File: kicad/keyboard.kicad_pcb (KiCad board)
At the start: 2 copper layers, 141 x 130.1 mm, 70 parts

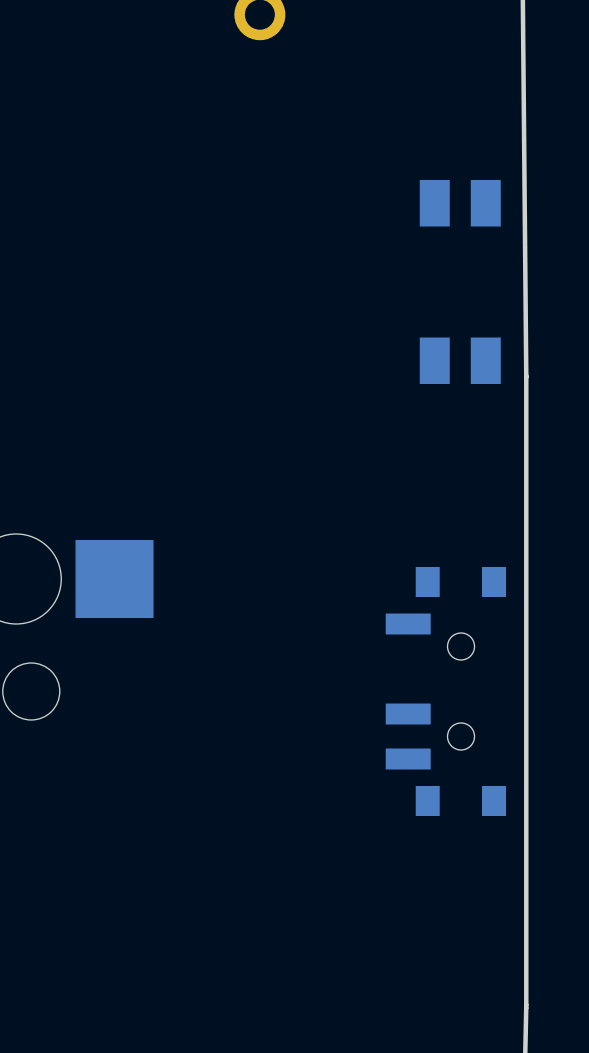
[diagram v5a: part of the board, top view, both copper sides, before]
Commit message: Move power/reset switches to Front; use detailed encoder WRL model
- power_switch and reset switch: side B -> F so they mount on the front
  (opposite the choc keys/hotswaps) and are accessible from that side.
- Replace crude Cosmos key-evqwgd001.step block with the detailed
  switch-evqwgd001 mesh converted to WRL. kicad-cli's raytracer does not
  render STL, so the STL was converted to VRML (coords pre-scaled by
  1/2.54 to compensate for KiCad's WRL unit factor). The encoder now
  renders as a realistic EVQWGD001 with visible roller wheel.
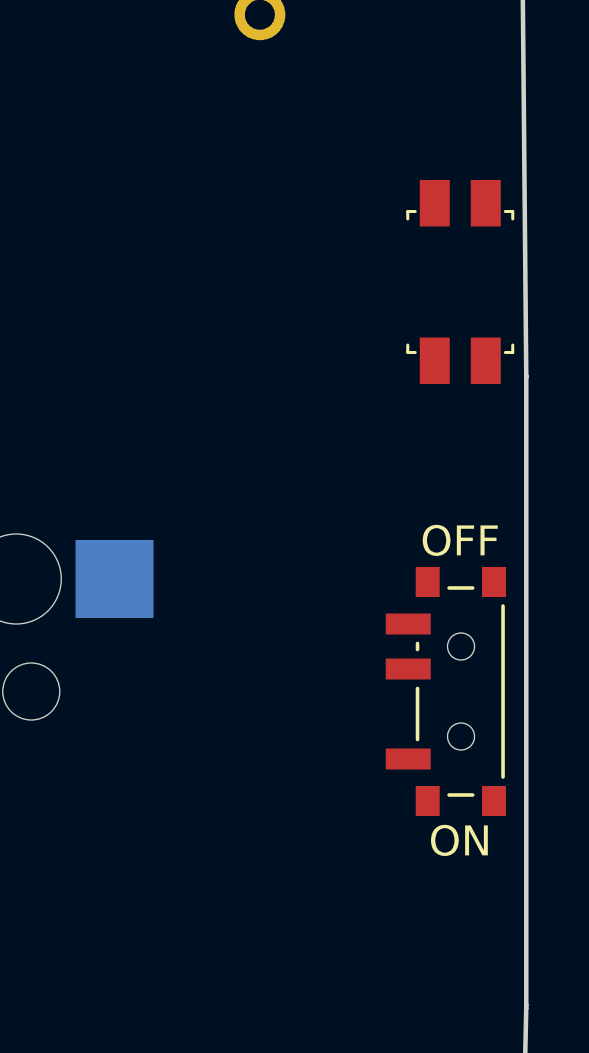
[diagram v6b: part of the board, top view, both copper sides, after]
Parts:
- PWR1, RST1: moved to F.Cu
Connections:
- PWR1 pad 1: (no net) -> BAT_P
- PWR1 pad 3: BAT_P -> (no net)
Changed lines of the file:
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@@
       (pad "D" thru_hole circle (at 5.625 3.81 0) (size 1.6 1.6) (drill 0.9) (layers "*.Cu" "*.Mask") (net 3 "GND"))
       (pad "" np_thru_hole circle (at 5.625 6.3 0) (size 1.5 1.5) (drill 1.5) (layers "*.Cu" "*.Mask"))
-    (model ${KIPRJMOD}/3d_models/EVQWGD001_Encoder.step
+    (model ${KIPRJMOD}/3d_models/EVQWGD001_Encoder.wrl
       (offset (xyz 0 0 0))
       (scale (xyz 1 1 1))
@@
     )
   (footprint "ceoloide:power_switch_smd_side"
-    (layer "B.Cu")
+    (layer "F.Cu")
     (at 153.8 77.5 0)
     (property "Reference" "PWR1"
       (at -3.6 0 -90)
-      (layer "B.SilkS")
+      (layer "F.SilkS")
       hide
       (effects (font (size 1 1) (thickness 0.15)))
     )
     (attr smd)
-    (fp_line (start 2.595 -0.1) (end 1.295 -0.1) (layer "B.Fab") (stroke (width 0.1) (type solid)))
-    (fp_line (start -1.305 3.35) (end -1.305 -3.35) (layer "B.Fab") (stroke (width 0.1) (type solid)))
-    (fp_line (start 2.645 -0.15) (end 2.595 -0.1) (layer "B.Fab") (stroke (width 0.1) (type solid)))
-    (fp_line (start 2.845 -1.2) (end 2.845 -0.35) (layer "B.Fab") (stroke (width 0.1) (type solid)))
-    (fp_line (start 1.345 -1.4) (end 2.645 -1.4) (layer "B.Fab") (stroke (width 0.1) (type solid)))
-    (fp_line (start 2.845 -0.35) (end 2.645 -0.15) (layer "B.Fab") (stroke (width 0.1) (type solid)))
-    (fp_line (start 2.645 -1.4) (end 2.845 -1.2) (layer "B.Fab") (stroke (width 0.1) (type solid)))
-    (fp_line (start 1.295 -3.35) (end 1.295 3.35) (layer "B.Fab") (stroke (width 0.1) (type solid)))
-    (fp_line (start 1.295 3.35) (end -1.305 3.35) (layer "B.Fab") (stroke (width 0.1) (type solid)))
-    (fp_line (start -1.305 -3.35) (end 1.295 -3.35) (layer "B.Fab") (stroke (width 0.1) (type solid)))
-    (pad "" smd rect (at -1.085 -3.65 270) (size 1 0.8) (layers "B.Cu" "B.Paste" "B.Mask"))
-    (pad "" smd rect (at 1.125 -3.65 270) (size 1 0.8) (layers "B.Cu" "B.Paste" "B.Mask"))
-    (pad "" smd rect (at -1.085 3.65 270) (size 1 0.8) (layers "B.Cu" "B.Paste" "B.Mask"))
-    (pad "" smd rect (at 1.125 3.65 270) (size 1 0.8) (layers "B.Cu" "B.Paste" "B.Mask"))
-    (pad "1" smd rect (at -1.735 -2.25 270) (size 0.7 1.5) (layers "B.Cu" "B.Paste" "B.Mask") )
-    (pad "2" smd rect (at -1.735 0.75 270) (size 0.7 1.5) (layers "B.Cu" "B.Paste" "B.Mask") (net 45 "RAW"))
-    (pad "3" smd rect (at -1.735 2.25 270) (size 0.7 1.5) (layers "B.Cu" "B.Paste" "B.Mask") (net 82 "BAT_P"))
-    (fp_text user "PWR1" (at -3.5 0 90) (layer "B.SilkS") hide
-      (effects (font (size 1 1) (thickness 0.15)) (justify mirror))
+    (fp_line (start -1.305 -3.35) (end -1.305 3.35) (layer "F.Fab") (stroke (width 0.1) (type solid)))
+    (fp_line (start 1.295 -3.35) (end -1.305 -3.35) (layer "F.Fab") (stroke (width 0.1) (type solid)))
+    (fp_line (start 1.295 3.35) (end 1.295 -3.35) (layer "F.Fab") (stroke (width 0.1) (type solid)))
+    (fp_line (start -1.305 3.35) (end 1.295 3.35) (layer "F.Fab") (stroke (width 0.1) (type solid)))
+    (fp_line (start 2.595 0.1) (end 1.295 0.1) (layer "F.Fab") (stroke (width 0.1) (type solid)))
+    (fp_line (start 2.645 0.15) (end 2.595 0.1) (layer "F.Fab") (stroke (width 0.1) (type solid)))
+    (fp_line (start 2.845 0.35) (end 2.645 0.15) (layer "F.Fab") (stroke (width 0.1) (type solid)))
+    (fp_line (start 2.845 1.2) (end 2.845 0.35) (layer "F.Fab") (stroke (width 0.1) (type solid)))
+    (fp_line (start 2.645 1.4) (end 2.845 1.2) (layer "F.Fab") (stroke (width 0.1) (type solid)))
+    (fp_line (start 1.345 1.4) (end 2.645 1.4) (layer "F.Fab") (stroke (width 0.1) (type solid)))
+    (pad "" smd rect (at 1.125 -3.65 90) (size 1 0.8) (layers "F.Cu" "F.Paste" "F.Mask"))
+    (pad "" smd rect (at -1.085 -3.65 90) (size 1 0.8) (layers "F.Cu" "F.Paste" "F.Mask"))
+    (pad "" smd rect (at -1.085 3.65 90) (size 1 0.8) (layers "F.Cu" "F.Paste" "F.Mask"))
+    (pad "" smd rect (at 1.125 3.65 90) (size 1 0.8) (layers "F.Cu" "F.Paste" "F.Mask"))
+    (pad "1" smd rect (at -1.735 2.25 90) (size 0.7 1.5) (layers "F.Cu" "F.Paste" "F.Mask") (net 82 "BAT_P"))
+    (pad "2" smd rect (at -1.735 -0.75 90) (size 0.7 1.5) (layers "F.Cu" "F.Paste" "F.Mask") (net 45 "RAW"))
+    (pad "3" smd rect (at -1.735 -2.25 90) (size 0.7 1.5) (layers "F.Cu" "F.Paste" "F.Mask") )
+    (fp_text user "ON" (at 0 5 0) (layer "F.SilkS")
+      (effects (font (size 1 1) (thickness 0.15)))
     )
-    (fp_text user "ON" (at 0 5 0) (layer "B.SilkS")
-      (effects (font (size 1 1) (thickness 0.15)) (justify mirror))
+    (fp_text user "OFF" (at 0 -5 0) (layer "F.SilkS")
+      (effects (font (size 1 1) (thickness 0.15)))
     )
-    (fp_text user "OFF" (at 0 -5 0) (layer "B.SilkS")
-      (effects (font (size 1 1) (thickness 0.15)) (justify mirror))
-    )
-    (fp_line (start -1.425 1.4) (end -1.425 1.6) (layer "B.SilkS") (stroke (width 0.12) (type solid)))
-    (fp_line (start 0.415 3.45) (end -0.375 3.45) (layer "B.SilkS") (stroke (width 0.12) (type solid)))
-    (fp_line (start -0.375 -3.45) (end 0.415 -3.45) (layer "B.SilkS") (stroke (width 0.12) (type solid)))
-    (fp_line (start -1.425 -1.6) (end -1.425 0.1) (layer "B.SilkS") (stroke (width 0.12) (type solid)))
-    (fp_line (start 1.425 -2.85) (end 1.425 2.85) (layer "B.SilkS") (stroke (width 0.12) (type solid)))
+    (fp_line (start 0.415 -3.45) (end -0.375 -3.45) (layer "F.SilkS") (stroke (width 0.12) (type solid)))
+    (fp_line (start -0.375 3.45) (end 0.415 3.45) (layer "F.SilkS") (stroke (width 0.12) (type solid)))
+    (fp_line (start -1.425 1.6) (end -1.425 -0.1) (layer "F.SilkS") (stroke (width 0.12) (type solid)))
+    (fp_line (start 1.425 2.85) (end 1.425 -2.85) (layer "F.SilkS") (stroke (width 0.12) (type solid)))
+    (fp_line (start -1.425 -1.4) (end -1.425 -1.6) (layer "F.SilkS") (stroke (width 0.12) (type solid)))
     (model ${KIPRJMOD}/3d_models/Switch_Power.step
-      (offset (xyz 0 0 -1.6))
+      (offset (xyz 0 0 0))
       (scale (xyz 1 1 1))
       (rotate (xyz 90 0 90))
@@
   )
   (footprint "ceoloide:reset_switch_smd_side"
-    (layer "B.Cu")
+    (layer "F.Cu")
     (at 153.8 63.85 -90)
     (property "Reference" "RST1"
       (at 0 0 -90)
-      (layer "B.SilkS")
+      (layer "F.SilkS")
       hide
       (effects (font (size 1 1) (thickness 0.15)))
@@
     (fp_line (start 1.3 -2.75) (end 1.3 -1.75) (stroke (width 0.1) (type solid)) (layer "Dwgs.User"))
     (fp_line (start 2.35 -1.75) (end 2.35 1.75) (stroke (width 0.1) (type solid)) (layer "Dwgs.User"))
-    (pad "1" smd rect (at -2.625 -0.85 90) (size 1.55 1) (layers "B.Cu" "B.Paste" "B.Mask") (net 3 "GND"))
-    (pad "2" smd rect (at -2.625 0.85 90) (size 1.55 1) (layers "B.Cu" "B.Paste" "B.Mask") (net 46 "RST"))
-    (pad "3" smd rect (at 2.625 -0.85 90) (size 1.55 1) (layers "B.Cu" "B.Paste" "B.Mask") (net 3 "GND"))
-    (pad "4" smd rect (at 2.625 0.85 90) (size 1.55 1) (layers "B.Cu" "B.Paste" "B.Mask") (net 46 "RST"))
-    (fp_line (start -2.35 -1.5) (end -2.35 -1.75) (stroke (width 0.1) (type solid)) (layer "B.SilkS"))
-    (fp_line (start -2.35 1.5) (end -2.35 1.75) (stroke (width 0.1) (type solid)) (layer "B.SilkS"))
-    (fp_line (start -2.1 -1.75) (end -2.35 -1.75) (stroke (width 0.1) (type solid)) (layer "B.SilkS"))
-    (fp_line (start -2.1 1.75) (end -2.35 1.75) (stroke (width 0.1) (type solid)) (layer "B.SilkS"))
-    (fp_line (start 2.1 -1.75) (end 2.35 -1.75) (stroke (width 0.1) (type solid)) (layer "B.SilkS"))
-    (fp_line (start 2.1 1.75) (end 2.35 1.75) (stroke (width 0.1) (type solid)) (layer "B.SilkS"))
-    (fp_line (start 2.35 -1.5) (end 2.35 -1.75) (stroke (width 0.1) (type solid)) (layer "B.SilkS"))
-    (fp_line (start 2.35 1.5) (end 2.35 1.75) (stroke (width 0.1) (type solid)) (layer "B.SilkS"))
+    (pad "1" smd rect (at 2.625 -0.85 90) (size 1.55 1) (layers "F.Cu" "F.Paste" "F.Mask") (net 3 "GND"))
+    (pad "2" smd rect (at 2.625 0.85 90) (size 1.55 1) (layers "F.Cu" "F.Paste" "F.Mask") (net 46 "RST"))
+    (pad "3" smd rect (at -2.625 -0.85 90) (size 1.55 1) (layers "F.Cu" "F.Paste" "F.Mask") (net 3 "GND"))
+    (pad "4" smd rect (at -2.625 0.85 90) (size 1.55 1) (layers "F.Cu" "F.Paste" "F.Mask") (net 46 "RST"))
+    (fp_line (start -2.35 -1.5) (end -2.35 -1.75) (stroke (width 0.1) (type solid)) (layer "F.SilkS"))
+    (fp_line (start -2.35 1.5) (end -2.35 1.75) (stroke (width 0.1) (type solid)) (layer "F.SilkS"))
+    (fp_line (start -2.1 -1.75) (end -2.35 -1.75) (stroke (width 0.1) (type solid)) (layer "F.SilkS"))
+    (fp_line (start -2.1 1.75) (end -2.35 1.75) (stroke (width 0.1) (type solid)) (layer "F.SilkS"))
+    (fp_line (start 2.1 -1.75) (end 2.35 -1.75) (stroke (width 0.1) (type solid)) (layer "F.SilkS"))
+    (fp_line (start 2.1 1.75) (end 2.35 1.75) (stroke (width 0.1) (type solid)) (layer "F.SilkS"))
+    (fp_line (start 2.35 -1.5) (end 2.35 -1.75) (stroke (width 0.1) (type solid)) (layer "F.SilkS"))
+    (fp_line (start 2.35 1.5) (end 2.35 1.75) (stroke (width 0.1) (type solid)) (layer "F.SilkS"))
     (model ${KIPRJMOD}/3d_models/Switch_Reset.step
       (offset (xyz 0 0 0))

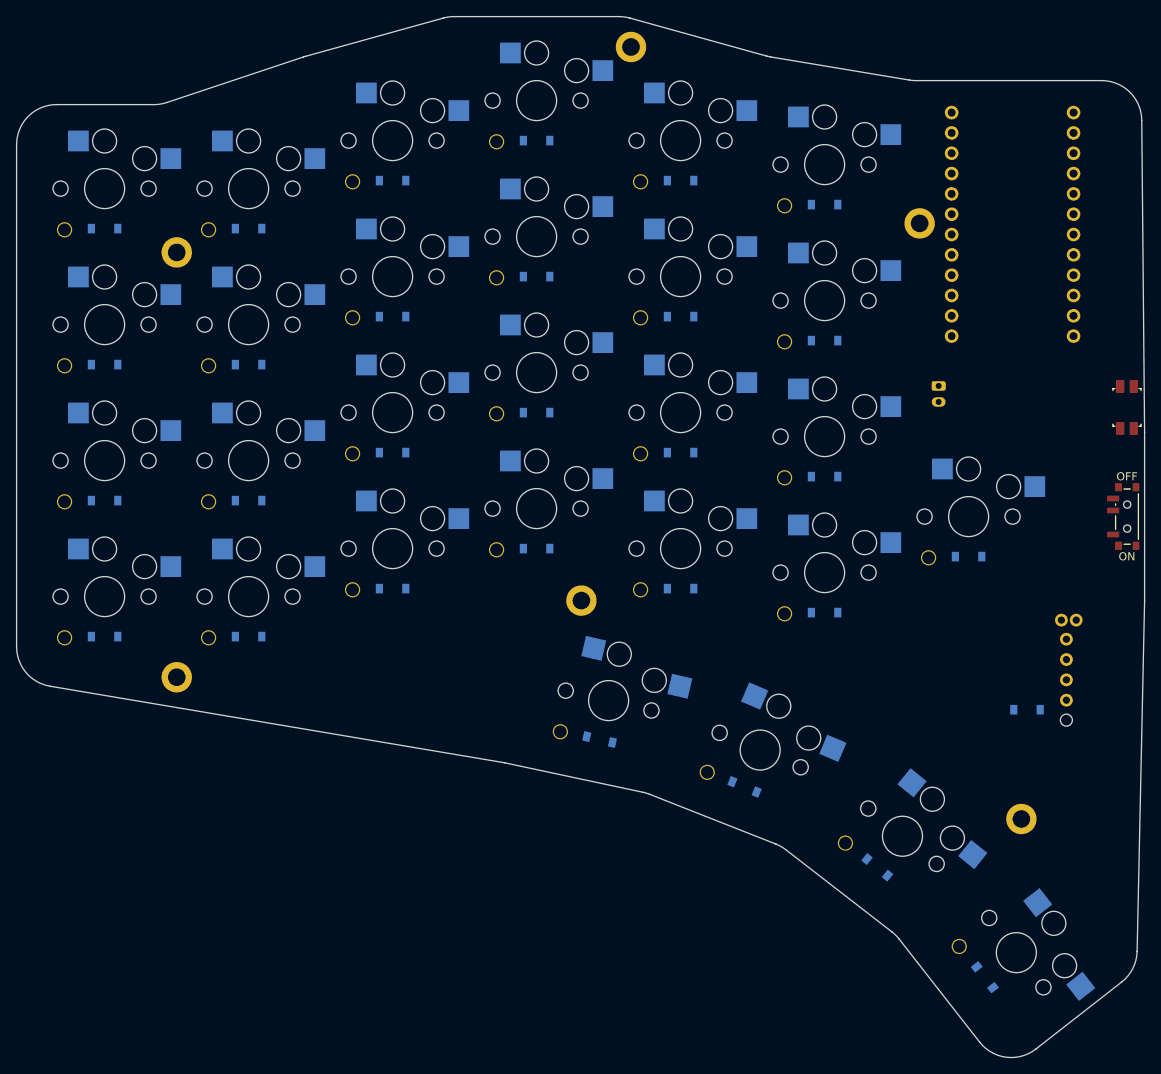
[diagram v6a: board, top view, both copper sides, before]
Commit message: Fix via annular DRU rule, nice!nano silk labels; align rules to JLC minimums
- Relax JLC_via_annular_ring DRU rule to 0.05mm: 0.45mm-via/0.3mm-hole is a
  standard no-extra-cost JLCPCB via; the 0.13mm annular guideline is for
  component PTH pads, not tented vias. Clears 75 false annular-ring errors.
- Move nice!nano silkscreen pin labels inward (4.47 -> 3.4mm) in the footprint
  source and in the routed PCB, clearing 4 silk-to-pad / silk-over-copper
  warnings (ENC1_C/ENC1_A were clipping the socket pads). Routing preserved.
- Align .kicad_pro constraints to JLCPCB's true 1oz 2-layer minimums (0.1mm
  track/space, 0.1mm hole-to-copper, 0.2mm copper-to-edge) so the routed board
  passes; the router's 'Fix DRC settings after routing' had loosened them.
- Document the rules (and the router-overwrite caveat) in README; gitignore
  KiCad *-drc.rpt files.

Final DRC: 0 errors, 0 unconnected. Board is JLCPCB-manufacturable.
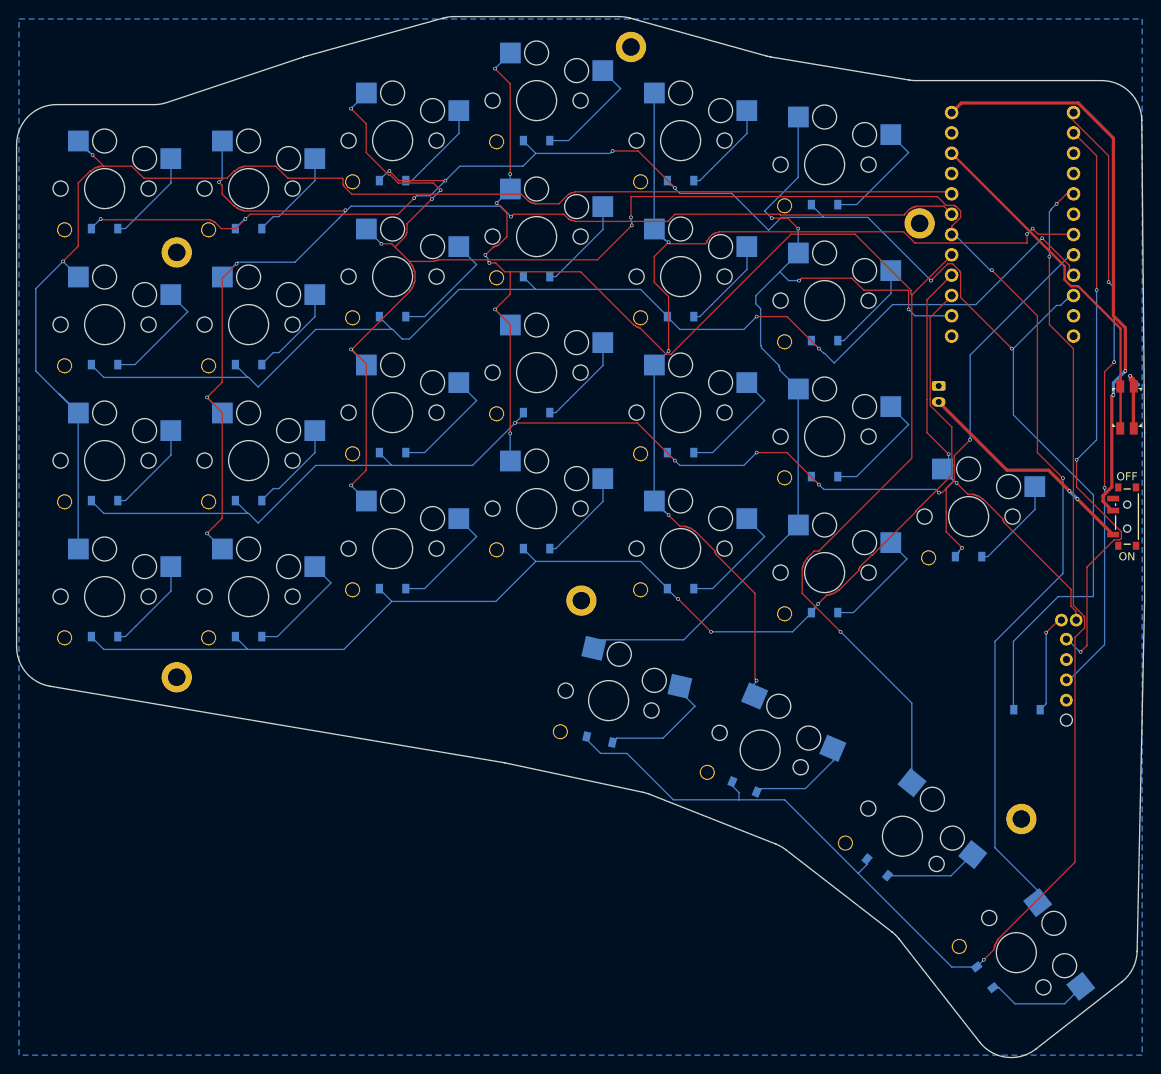
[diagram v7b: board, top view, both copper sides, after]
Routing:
- net P19: track 0.00 -> 249.7 mm, vias 0 -> 10
- net P11: track 0.00 -> 218.6 mm, vias 0 -> 9
- net P18: track 0.00 -> 205.8 mm, vias 0 -> 8
- net P21: track 0.00 -> 175.2 mm, vias 0 -> 2
- net P13: track 0.00 -> 173.5 mm, vias 0 -> 7
- net P2: track 0.00 -> 171.6 mm, vias 0 -> 3
- net P20: track 0.00 -> 163.3 mm, vias 0 -> 6
- net P14: track 0.00 -> 155.9 mm, vias 0 -> 3
- net P12: track 0.00 -> 152.3 mm, vias 0 -> 3
- net P17: track 0.00 -> 138.5 mm, vias 0 -> 6
- net P16: track 0.00 -> 117.4 mm, vias 0 -> 4
- net ENC1_C: track 0.00 -> 75.7 mm, vias 0 -> 3
- net ENC1_A: track 0.00 -> 74.2 mm, vias 0 -> 3
- net RAW: track 0.00 -> 71.6 mm, vias 0 -> 2
- net P15: track 0.00 -> 53.7 mm, vias 0 -> 2
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- added copper zone on B.Cu, net GND
